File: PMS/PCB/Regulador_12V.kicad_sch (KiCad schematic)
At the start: 14 parts, among them U4 MP2303ADN

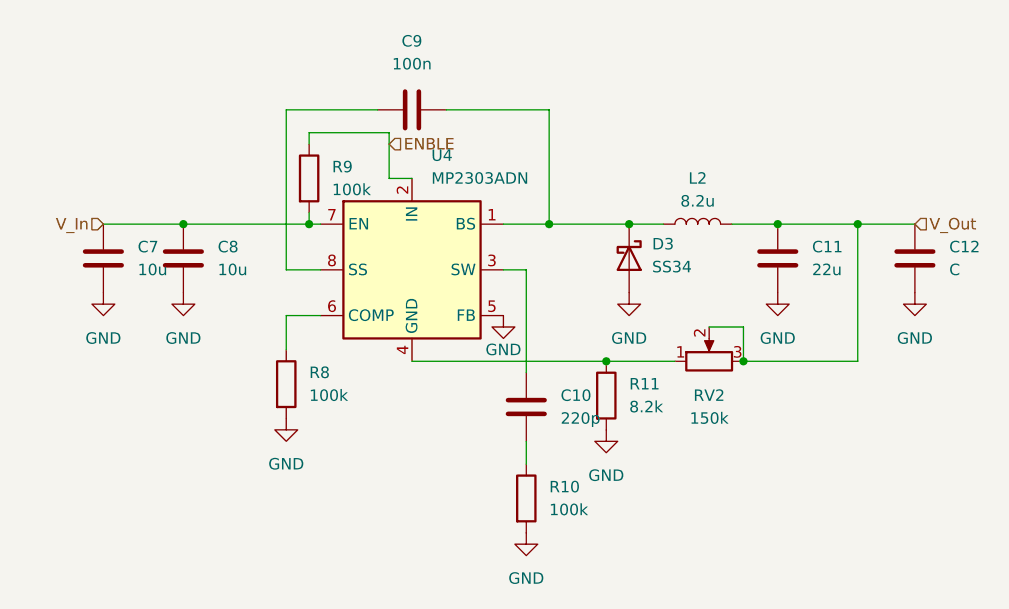
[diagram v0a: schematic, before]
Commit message: Define ciertos pines y diseña mediciones
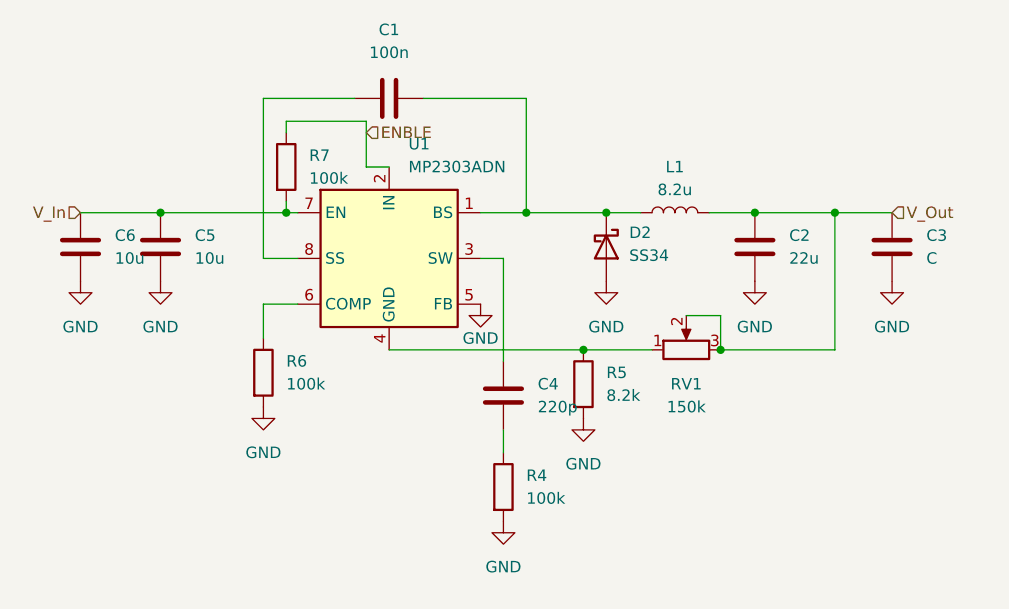
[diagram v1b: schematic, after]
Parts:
- removed C10: 220p, symbol Device:C
- removed C11: 22u, symbol Device:C
- removed C12: C, symbol Device:C
- removed C7, C8: 10u, symbol Device:C
- removed C9: 100n, symbol Device:C
- removed D3: SS34, Diode_SMD:D_SMA, symbol Diode:SS34
- removed L2: 8.2u, symbol Device:L
- removed R10, R8, R9: 100k, symbol Device:R
- removed R11: 8.2k, symbol Device:R
- removed RV2: 150k, symbol Device:R_Potentiometer
- removed U4: MP2303ADN, Package_SO:SOIC-8-1EP_3.9x4.9mm_P1.27mm_EP2.62x3.51mm, symbol Regulator_Switching:MP2303ADN
- added C1: 100n, symbol Device:C
- added C2: 22u, symbol Device:C
- added C3: C, symbol Device:C
- added C4: 220p, symbol Device:C
- added C5, C6: 10u, symbol Device:C
- added D2: SS34, Diode_SMD:D_SMA, symbol Diode:SS34
- added L1: 8.2u, symbol Device:L
- added R4, R6, R7: 100k, symbol Device:R
- added R5: 8.2k, symbol Device:R
- added RV1: 150k, symbol Device:R_Potentiometer
- added U1: MP2303ADN, Package_SO:SOIC-8-1EP_3.9x4.9mm_P1.27mm_EP2.62x3.51mm, symbol Regulator_Switching:MP2303ADN
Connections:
- net ENBLE: now also R7.1, U1.2 (IN)
- net GND: now also C2.2, C3.2, C5.2, C6.2, D2.2 (A), R4.2, R5.2, R6.2, U1.5 (FB)
- net V_In: now also C5.1, C6.1, R7.2, U1.7 (EN)
- net V_Out: now also C2.1, C3.1, L1.2, RV1.2, RV1.3
- new net: C4.2, R4.1
- new net: C1.2, D2.1 (K), L1.1, U1.1 (BS)
- new net: C4.1, U1.3 (SW)
- new net: R5.1, RV1.1, U1.4 (GND)
- new net: R6.1, U1.6 (COMP)
- new net: C1.1, U1.8 (SS)
